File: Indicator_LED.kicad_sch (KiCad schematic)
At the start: 4 parts

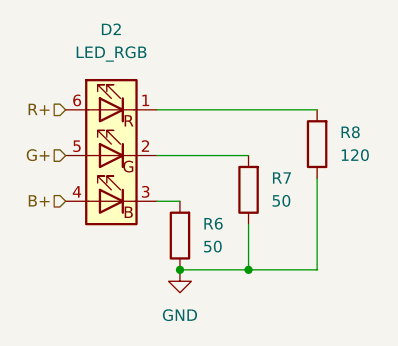
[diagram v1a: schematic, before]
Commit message: finished layout, routing, and silkscreen
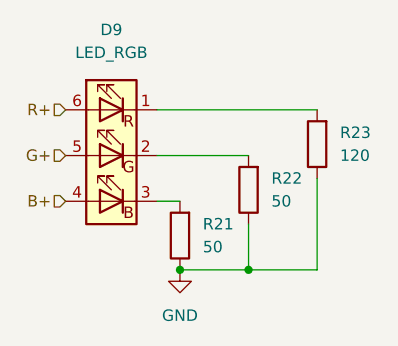
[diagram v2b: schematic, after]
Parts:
- renumbered D2 to D9, R6 to R21, R7 to R22, R8 to R23
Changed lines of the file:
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@@
 		(in_pos_files yes)
 		(dnp no)
-		(property "Reference" "R6"
+		(property "Reference" "R21"
 			(at 130.81 97.7899 0)
 			(show_name no)
@@
 			(project "RSC-LV3-LVBPS"
 				(path "/4bbf2fff-9f66-421d-84bf-68d1dcd1e11d/4b8add19-2d3e-4ee3-9fc6-a72eb5b6d291/60bb412c-fe9a-4662-b62c-205cebbf95f7"
-					(reference "R6")
+					(reference "R21")
 					(unit 1)
 				)
 				(path "/4bbf2fff-9f66-421d-84bf-68d1dcd1e11d/4b8add19-2d3e-4ee3-9fc6-a72eb5b6d291/ccdf9a5c-a31a-473f-8738-c18c4e0c4a96"
-					(reference "R9")
+					(reference "R24")
 					(unit 1)
 				)
@@
 		(in_pos_files yes)
 		(dnp no)
-		(property "Reference" "R7"
+		(property "Reference" "R22"
 			(at 138.43 92.7099 0)
 			(show_name no)
@@
 			(project "RSC-LV3-LVBPS"
 				(path "/4bbf2fff-9f66-421d-84bf-68d1dcd1e11d/4b8add19-2d3e-4ee3-9fc6-a72eb5b6d291/60bb412c-fe9a-4662-b62c-205cebbf95f7"
-					(reference "R7")
+					(reference "R22")
 					(unit 1)
 				)
 				(path "/4bbf2fff-9f66-421d-84bf-68d1dcd1e11d/4b8add19-2d3e-4ee3-9fc6-a72eb5b6d291/ccdf9a5c-a31a-473f-8738-c18c4e0c4a96"
-					(reference "R10")
+					(reference "R25")
 					(unit 1)
 				)
@@
 		(dnp no)
 		(fields_autoplaced yes)
-		(property "Reference" "#PWR026"
+		(property "Reference" "#PWR044"
 			(at 128.27 109.22 0)
 			(hide yes)
@@
 			(project "RSC-LV3-LVBPS"
 				(path "/4bbf2fff-9f66-421d-84bf-68d1dcd1e11d/4b8add19-2d3e-4ee3-9fc6-a72eb5b6d291/60bb412c-fe9a-4662-b62c-205cebbf95f7"
-					(reference "#PWR026")
+					(reference "#PWR044")
 					(unit 1)
 				)
 				(path "/4bbf2fff-9f66-421d-84bf-68d1dcd1e11d/4b8add19-2d3e-4ee3-9fc6-a72eb5b6d291/ccdf9a5c-a31a-473f-8738-c18c4e0c4a96"
-					(reference "#PWR027")
+					(reference "#PWR045")
 					(unit 1)
 				)
@@
 		(in_pos_files yes)
 		(dnp no)
-		(property "Reference" "R8"
+		(property "Reference" "R23"
 			(at 146.05 87.6299 0)
 			(show_name no)
@@
 			(project "RSC-LV3-LVBPS"
 				(path "/4bbf2fff-9f66-421d-84bf-68d1dcd1e11d/4b8add19-2d3e-4ee3-9fc6-a72eb5b6d291/60bb412c-fe9a-4662-b62c-205cebbf95f7"
-					(reference "R8")
+					(reference "R23")
 					(unit 1)
 				)
 				(path "/4bbf2fff-9f66-421d-84bf-68d1dcd1e11d/4b8add19-2d3e-4ee3-9fc6-a72eb5b6d291/ccdf9a5c-a31a-473f-8738-c18c4e0c4a96"
-					(reference "R11")
+					(reference "R26")
 					(unit 1)
 				)
@@
 		(dnp no)
 		(fields_autoplaced yes)
-		(property "Reference" "D2"
+		(property "Reference" "D9"
 			(at 120.65 76.2 0)
 			(show_name no)
@@
 			(project "RSC-LV3-LVBPS"
 				(path "/4bbf2fff-9f66-421d-84bf-68d1dcd1e11d/4b8add19-2d3e-4ee3-9fc6-a72eb5b6d291/60bb412c-fe9a-4662-b62c-205cebbf95f7"
-					(reference "D2")
+					(reference "D9")
 					(unit 1)
 				)
 				(path "/4bbf2fff-9f66-421d-84bf-68d1dcd1e11d/4b8add19-2d3e-4ee3-9fc6-a72eb5b6d291/ccdf9a5c-a31a-473f-8738-c18c4e0c4a96"
-					(reference "D3")
-					(unit 1)
-				)
+					(reference "D10")
+					(unit 1)
+				)
